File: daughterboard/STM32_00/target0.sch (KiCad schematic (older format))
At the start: 7 parts, among them U0 STM32G031F4P6

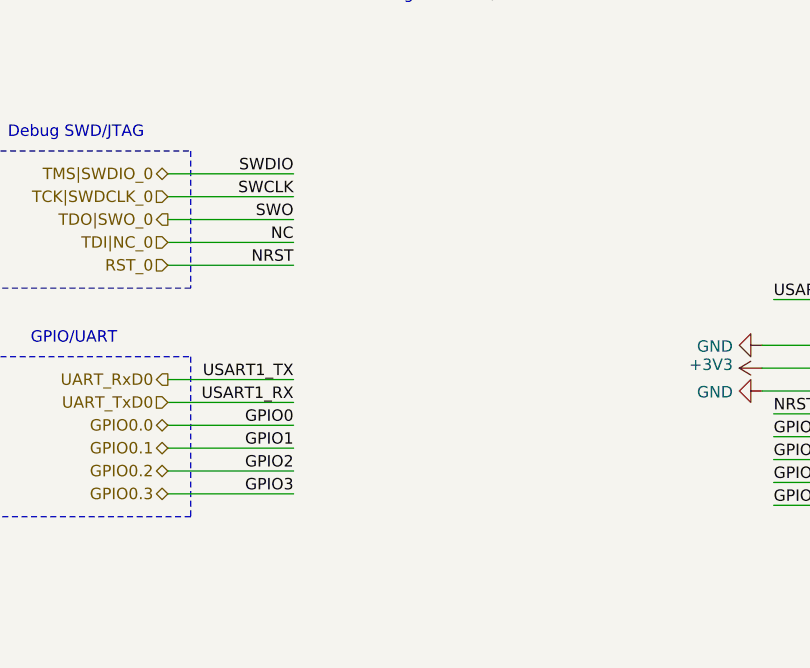
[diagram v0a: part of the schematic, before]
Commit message: added testpoints to daughterboards, updated readme
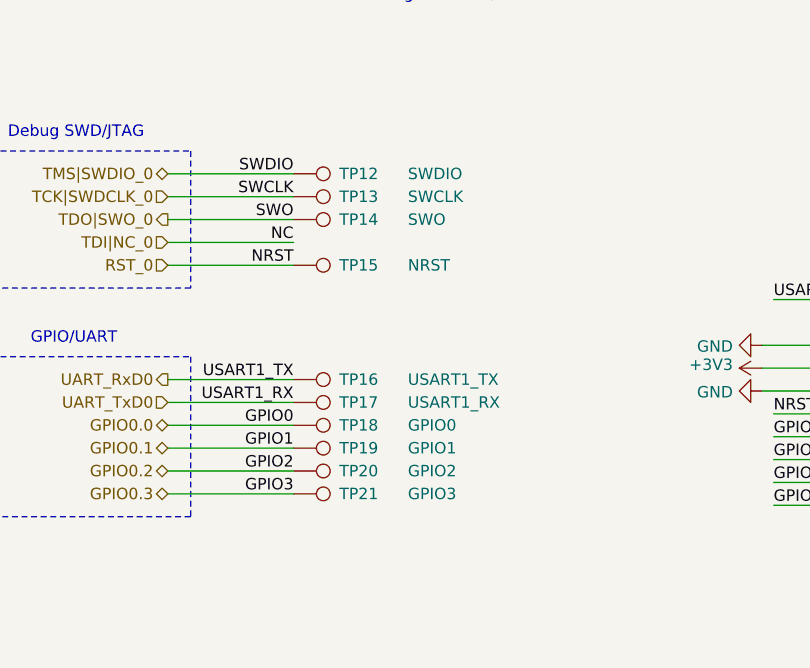
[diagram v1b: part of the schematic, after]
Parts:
- added TP12: SWDIO, symbol Connector:TestPoint
- added TP13: SWCLK, symbol Connector:TestPoint
- added TP14: SWO, symbol Connector:TestPoint
- added TP15: NRST, symbol Connector:TestPoint
- added TP16: USART1_TX, symbol Connector:TestPoint
- added TP17: USART1_RX, symbol Connector:TestPoint
- added TP18: GPIO0, symbol Connector:TestPoint
- added TP19: GPIO1, symbol Connector:TestPoint
- added TP20: GPIO2, symbol Connector:TestPoint
- added TP21: GPIO3, symbol Connector:TestPoint
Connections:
- net GPIO0.0: now also TP18.1
- net GPIO0.1: now also TP19.1
- net GPIO0.2: now also TP20.1
- net GPIO0.3: now also TP21.1
- net RST_0: now also TP15.1
- net TCK|SWDCLK_0: now also TP13.1
- net TDO|SWO_0: now also TP14.1
- net TMS|SWDIO_0: now also TP12.1
- net UART_RxD0: now also TP16.1
- net UART_TxD0: now also TP17.1
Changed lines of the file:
@@
 Wire Wire Line
 	9050 2800 9300 2800
+$Comp
+L Connector:TestPoint TP?
+U 1 1 6191E300
+P 2250 1650
+AR Path="/616688D6/6191E300" Ref="TP?"  Part="1"
+AR Path="/61668514/6191E300" Ref="TP12"  Part="1"
+F 0 "TP12" V 2250 1850 50  0000 L CNN
+F 1 "SWDIO" V 2250 2150 50  0000 L CNN
+F 2 "" H 2450 1650 50  0001 C CNN
+F 3 "~" H 2450 1650 50  0001 C CNN
+	1    2250 1650
+	0    1    1    0
+$EndComp
+$Comp
+L Connector:TestPoint TP?
+U 1 1 6191E306
+P 2250 1750
+AR Path="/616688D6/6191E306" Ref="TP?"  Part="1"
+AR Path="/61668514/6191E306" Ref="TP13"  Part="1"
+F 0 "TP13" V 2250 1950 50  0000 L CNN
+F 1 "SWCLK" V 2250 2250 50  0000 L CNN
+F 2 "" H 2450 1750 50  0001 C CNN
+F 3 "~" H 2450 1750 50  0001 C CNN
+	1    2250 1750
+	0    1    1    0
+$EndComp
+$Comp
+L Connector:TestPoint TP?
+U 1 1 6191E30C
+P 2250 1850
+AR Path="/616688D6/6191E30C" Ref="TP?"  Part="1"
+AR Path="/61668514/6191E30C" Ref="TP14"  Part="1"
+F 0 "TP14" V 2250 2050 50  0000 L CNN
+F 1 "SWO" V 2250 2350 50  0000 L CNN
+F 2 "" H 2450 1850 50  0001 C CNN
+F 3 "~" H 2450 1850 50  0001 C CNN
+	1    2250 1850
+	0    1    1    0
+$EndComp
+$Comp
+L Connector:TestPoint TP?
+U 1 1 6191E318
+P 2250 2050
+AR Path="/616688D6/6191E318" Ref="TP?"  Part="1"
+AR Path="/61668514/6191E318" Ref="TP15"  Part="1"
+F 0 "TP15" V 2250 2250 50  0000 L CNN
+F 1 "NRST" V 2250 2550 50  0000 L CNN
+F 2 "" H 2450 2050 50  0001 C CNN
+F 3 "~" H 2450 2050 50  0001 C CNN
+	1    2250 2050
+	0    1    1    0
+$EndComp
+$Comp
+L Connector:TestPoint TP?
+U 1 1 6191E31E
+P 2250 2550
+AR Path="/616688D6/6191E31E" Ref="TP?"  Part="1"
+AR Path="/61668514/6191E31E" Ref="TP16"  Part="1"
+F 0 "TP16" V 2250 2750 50  0000 L CNN
+F 1 "USART1_TX" V 2250 3050 50  0000 L CNN
+F 2 "" H 2450 2550 50  0001 C CNN
+F 3 "~" H 2450 2550 50  0001 C CNN
+	1    2250 2550
+	0    1    1    0
+$EndComp
+$Comp
+L Connector:TestPoint TP?
+U 1 1 6191E324
+P 2250 2650
+AR Path="/616688D6/6191E324" Ref="TP?"  Part="1"
+AR Path="/61668514/6191E324" Ref="TP17"  Part="1"
+F 0 "TP17" V 2250 2850 50  0000 L CNN
+F 1 "USART1_RX" V 2250 3150 50  0000 L CNN
+F 2 "" H 2450 2650 50  0001 C CNN
+F 3 "~" H 2450 2650 50  0001 C CNN
+	1    2250 2650
+	0    1    1    0
+$EndComp
+$Comp
+L Connector:TestPoint TP?
+U 1 1 6191E32A
+P 2250 2750
+AR Path="/616688D6/6191E32A" Ref="TP?"  Part="1"
+AR Path="/61668514/6191E32A" Ref="TP18"  Part="1"
+F 0 "TP18" V 2250 2950 50  0000 L CNN
+F 1 "GPIO0" V 2250 3250 50  0000 L CNN
+F 2 "" H 2450 2750 50  0001 C CNN
+F 3 "~" H 2450 2750 50  0001 C CNN
+	1    2250 2750
+	0    1    1    0
+$EndComp
+$Comp
+L Connector:TestPoint TP?
+U 1 1 6191E330
+P 2250 2850
+AR Path="/616688D6/6191E330" Ref="TP?"  Part="1"
+AR Path="/61668514/6191E330" Ref="TP19"  Part="1"
+F 0 "TP19" V 2250 3050 50  0000 L CNN
+F 1 "GPIO1" V 2250 3350 50  0000 L CNN
+F 2 "" H 2450 2850 50  0001 C CNN
+F 3 "~" H 2450 2850 50  0001 C CNN
+	1    2250 2850
+	0    1    1    0
+$EndComp
+$Comp
+L Connector:TestPoint TP?
+U 1 1 6191E336
+P 2250 2950
+AR Path="/616688D6/6191E336" Ref="TP?"  Part="1"
+AR Path="/61668514/6191E336" Ref="TP20"  Part="1"
+F 0 "TP20" V 2250 3150 50  0000 L CNN
+F 1 "GPIO2" V 2250 3450 50  0000 L CNN
+F 2 "" H 2450 2950 50  0001 C CNN
+F 3 "~" H 2450 2950 50  0001 C CNN
+	1    2250 2950
+	0    1    1    0
+$EndComp
+$Comp
+L Connector:TestPoint TP?
+U 1 1 6191E33C
+P 2250 3050
+AR Path="/616688D6/6191E33C" Ref="TP?"  Part="1"
+AR Path="/61668514/6191E33C" Ref="TP21"  Part="1"
+F 0 "TP21" V 2250 3250 50  0000 L CNN
+F 1 "GPIO3" V 2250 3550 50  0000 L CNN
+F 2 "" H 2450 3050 50  0001 C CNN
+F 3 "~" H 2450 3050 50  0001 C CNN
+	1    2250 3050
+	0    1    1    0
+$EndComp
 $EndSCHEMATC

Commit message: finished layout of STM32 daughterboard
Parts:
- removed TP14: SWO, symbol Connector:TestPoint
- removed TP15: NRST, symbol Connector:TestPoint
- removed TP18: GPIO0, symbol Connector:TestPoint
- removed TP19: GPIO1, symbol Connector:TestPoint
- removed TP20: GPIO2, symbol Connector:TestPoint
- removed TP21: GPIO3, symbol Connector:TestPoint
- C10, C11, C9: footprint (none) -> Capacitor_SMD:C_0603_1608Metric_Pad1.05x0.95mm_HandSolder
- JP3: footprint (none) -> Jumper:SolderJumper-2_P1.3mm_Open_TrianglePad1.0x1.5mm
- R2, R3: footprint (none) -> Resistor_SMD:R_0603_1608Metric_Pad1.05x0.95mm_HandSolder
- TP12, TP13, TP16, TP17: footprint (none) -> TestPoint:TestPoint_Pad_1.0x1.0mm
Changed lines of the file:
@@
 F 0 "C10" H 9142 2646 50  0000 L CNN
 F 1 "100n" H 9142 2555 50  0000 L CNN
-F 2 "" H 9050 2600 50  0001 C CNN
+F 2 "Capacitor_SMD:C_0603_1608Metric_Pad1.05x0.95mm_HandSolder" H 9050 2600 50  0001 C CNN
 F 3 "~" H 9050 2600 50  0001 C CNN
 	1    9050 2600
@@
 F 0 "C11" H 9642 2646 50  0000 L CNN
 F 1 "4.7u" H 9642 2555 50  0000 L CNN
-F 2 "" H 9550 2600 50  0001 C CNN
+F 2 "Capacitor_SMD:C_0603_1608Metric_Pad1.05x0.95mm_HandSolder" H 9550 2600 50  0001 C CNN
 F 3 "~" H 9550 2600 50  0001 C CNN
 	1    9550 2600
@@
 F 0 "R2" H 1109 6996 50  0000 L CNN
 F 1 "100k" H 1109 6905 50  0000 L CNN
-F 2 "" H 1050 6950 50  0001 C CNN
+F 2 "Resistor_SMD:R_0603_1608Metric_Pad1.05x0.95mm_HandSolder" H 1050 6950 50  0001 C CNN
 F 3 "~" H 1050 6950 50  0001 C CNN
 	1    1050 6950
@@
 F 0 "R3" H 1559 6996 50  0000 L CNN
 F 1 "100k" H 1559 6905 50  0000 L CNN
-F 2 "" H 1500 6950 50  0001 C CNN
+F 2 "Resistor_SMD:R_0603_1608Metric_Pad1.05x0.95mm_HandSolder" H 1500 6950 50  0001 C CNN
 F 3 "~" H 1500 6950 50  0001 C CNN
 	1    1500 6950
@@
 F 0 "C9" H 1142 5046 50  0000 L CNN
 F 1 "100n" H 1142 4955 50  0000 L CNN
-F 2 "" H 1050 5000 50  0001 C CNN
+F 2 "Capacitor_SMD:C_0603_1608Metric_Pad1.05x0.95mm_HandSolder" H 1050 5000 50  0001 C CNN
 F 3 "~" H 1050 5000 50  0001 C CNN
 	1    1050 5000
@@
 F 0 "JP3" V 1596 4912 50  0000 R CNN
 F 1 "NRST0" V 1505 4912 50  0000 R CNN
-F 2 "" H 1550 5000 50  0001 C CNN
+F 2 "Jumper:SolderJumper-2_P1.3mm_Open_TrianglePad1.0x1.5mm" H 1550 5000 50  0001 C CNN
 F 3 "~" H 1550 5000 50  0001 C CNN
 	1    1550 5000
@@
 F 0 "TP12" V 2250 1850 50  0000 L CNN
 F 1 "SWDIO" V 2250 2150 50  0000 L CNN
-F 2 "" H 2450 1650 50  0001 C CNN
+F 2 "TestPoint:TestPoint_Pad_1.0x1.0mm" H 2450 1650 50  0001 C CNN
 F 3 "~" H 2450 1650 50  0001 C CNN
 	1    2250 1650
@@
 F 0 "TP13" V 2250 1950 50  0000 L CNN
 F 1 "SWCLK" V 2250 2250 50  0000 L CNN
-F 2 "" H 2450 1750 50  0001 C CNN
+F 2 "TestPoint:TestPoint_Pad_1.0x1.0mm" H 2450 1750 50  0001 C CNN
 F 3 "~" H 2450 1750 50  0001 C CNN
 	1    2250 1750
-	0    1    1    0
-$EndComp
-$Comp
-L Connector:TestPoint TP?
-U 1 1 6191E30C
-P 2250 1850
-AR Path="/616688D6/6191E30C" Ref="TP?"  Part="1"
-AR Path="/61668514/6191E30C" Ref="TP14"  Part="1"
-F 0 "TP14" V 2250 2050 50  0000 L CNN
-F 1 "SWO" V 2250 2350 50  0000 L CNN
-F 2 "" H 2450 1850 50  0001 C CNN
-F 3 "~" H 2450 1850 50  0001 C CNN
-	1    2250 1850
-	0    1    1    0
-$EndComp
-$Comp
-L Connector:TestPoint TP?
-U 1 1 6191E318
-P 2250 2050
-AR Path="/616688D6/6191E318" Ref="TP?"  Part="1"
-AR Path="/61668514/6191E318" Ref="TP15"  Part="1"
-F 0 "TP15" V 2250 2250 50  0000 L CNN
-F 1 "NRST" V 2250 2550 50  0000 L CNN
-F 2 "" H 2450 2050 50  0001 C CNN
-F 3 "~" H 2450 2050 50  0001 C CNN
-	1    2250 2050
 	0    1    1    0
 $EndComp
@@
 F 0 "TP16" V 2250 2750 50  0000 L CNN
 F 1 "USART1_TX" V 2250 3050 50  0000 L CNN
-F 2 "" H 2450 2550 50  0001 C CNN
+F 2 "TestPoint:TestPoint_Pad_1.0x1.0mm" H 2450 2550 50  0001 C CNN
 F 3 "~" H 2450 2550 50  0001 C CNN
 	1    2250 2550
@@
 F 0 "TP17" V 2250 2850 50  0000 L CNN
 F 1 "USART1_RX" V 2250 3150 50  0000 L CNN
-F 2 "" H 2450 2650 50  0001 C CNN
+F 2 "TestPoint:TestPoint_Pad_1.0x1.0mm" H 2450 2650 50  0001 C CNN
 F 3 "~" H 2450 2650 50  0001 C CNN
 	1    2250 2650
 	0    1    1    0
 $EndComp
-$Comp
-L Connector:TestPoint TP?
-U 1 1 6191E32A
-P 2250 2750
-AR Path="/616688D6/6191E32A" Ref="TP?"  Part="1"
-AR Path="/61668514/6191E32A" Ref="TP18"  Part="1"
-F 0 "TP18" V 2250 2950 50  0000 L CNN
-F 1 "GPIO0" V 2250 3250 50  0000 L CNN
-F 2 "" H 2450 2750 50  0001 C CNN
-F 3 "~" H 2450 2750 50  0001 C CNN
-	1    2250 2750
-	0    1    1    0
-$EndComp
-$Comp
-L Connector:TestPoint TP?
-U 1 1 6191E330
-P 2250 2850
-AR Path="/616688D6/6191E330" Ref="TP?"  Part="1"
-AR Path="/61668514/6191E330" Ref="TP19"  Part="1"
-F 0 "TP19" V 2250 3050 50  0000 L CNN
-F 1 "GPIO1" V 2250 3350 50  0000 L CNN
-F 2 "" H 2450 2850 50  0001 C CNN
-F 3 "~" H 2450 2850 50  0001 C CNN
-	1    2250 2850
-	0    1    1    0
-$EndComp
-$Comp
-L Connector:TestPoint TP?
-U 1 1 6191E336
-P 2250 2950
-AR Path="/616688D6/6191E336" Ref="TP?"  Part="1"
-AR Path="/61668514/6191E336" Ref="TP20"  Part="1"
-F 0 "TP20" V 2250 3150 50  0000 L CNN
-F 1 "GPIO2" V 2250 3450 50  0000 L CNN
-F 2 "" H 2450 2950 50  0001 C CNN
-F 3 "~" H 2450 2950 50  0001 C CNN
-	1    2250 2950
-	0    1    1    0
-$EndComp
-$Comp
-L Connector:TestPoint TP?
-U 1 1 6191E33C
-P 2250 3050
-AR Path="/616688D6/6191E33C" Ref="TP?"  Part="1"
-AR Path="/61668514/6191E33C" Ref="TP21"  Part="1"
-F 0 "TP21" V 2250 3250 50  0000 L CNN
-F 1 "GPIO3" V 2250 3550 50  0000 L CNN
-F 2 "" H 2450 3050 50  0001 C CNN
-F 3 "~" H 2450 3050 50  0001 C CNN
-	1    2250 3050
-	0    1    1    0
-$EndComp
